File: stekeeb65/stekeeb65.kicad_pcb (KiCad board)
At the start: 2 copper layers, 303.2 x 97.6 mm, 251 parts, among them IC0 ATMEGA32U4-AU, IC1 IS31FL3733B-TQLS4, IC2 IS31FL3733B-TQLS4, J0 Conn_02x03_Odd_Even, J1 TYPE-C-31-M12_13_EDITED, SW0 SW_Push, U0 WE-TVS-82400102, Y0 16MHz

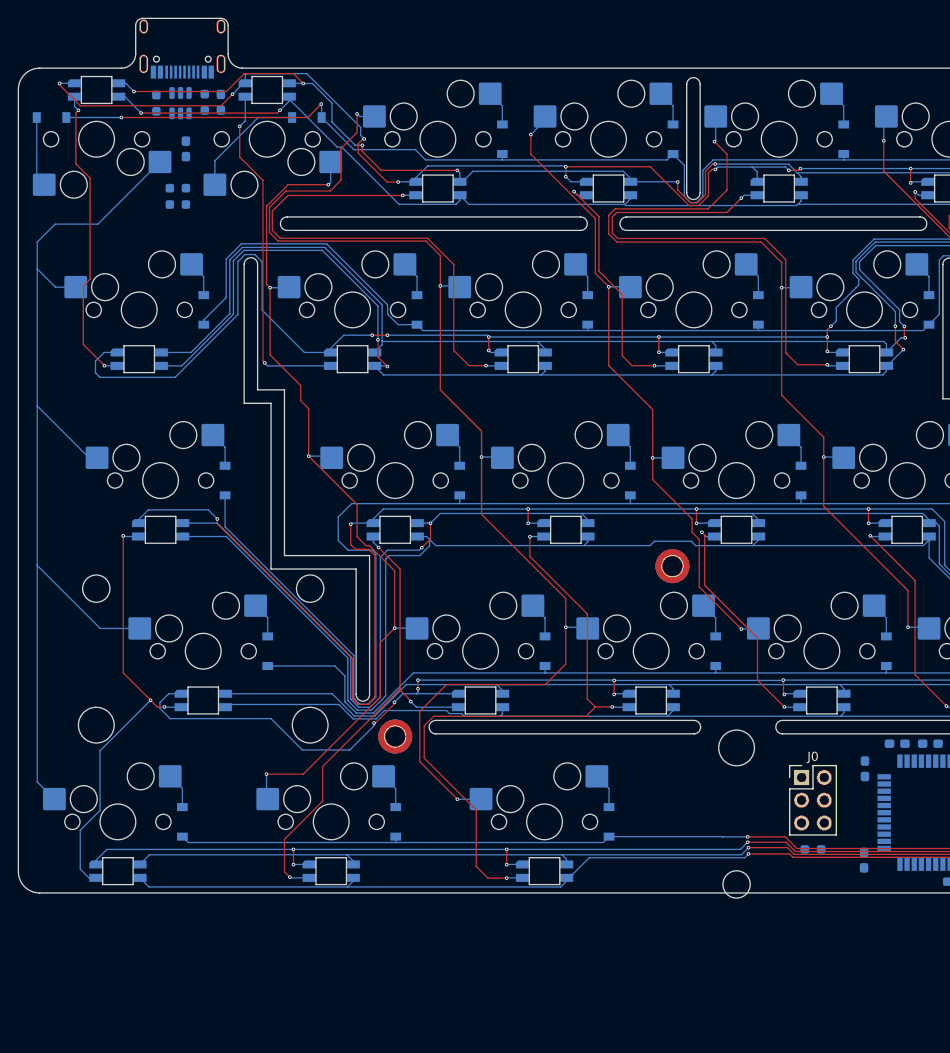
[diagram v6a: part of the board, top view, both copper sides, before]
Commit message: Replacing Type-C in lieu of a daughter board connector.
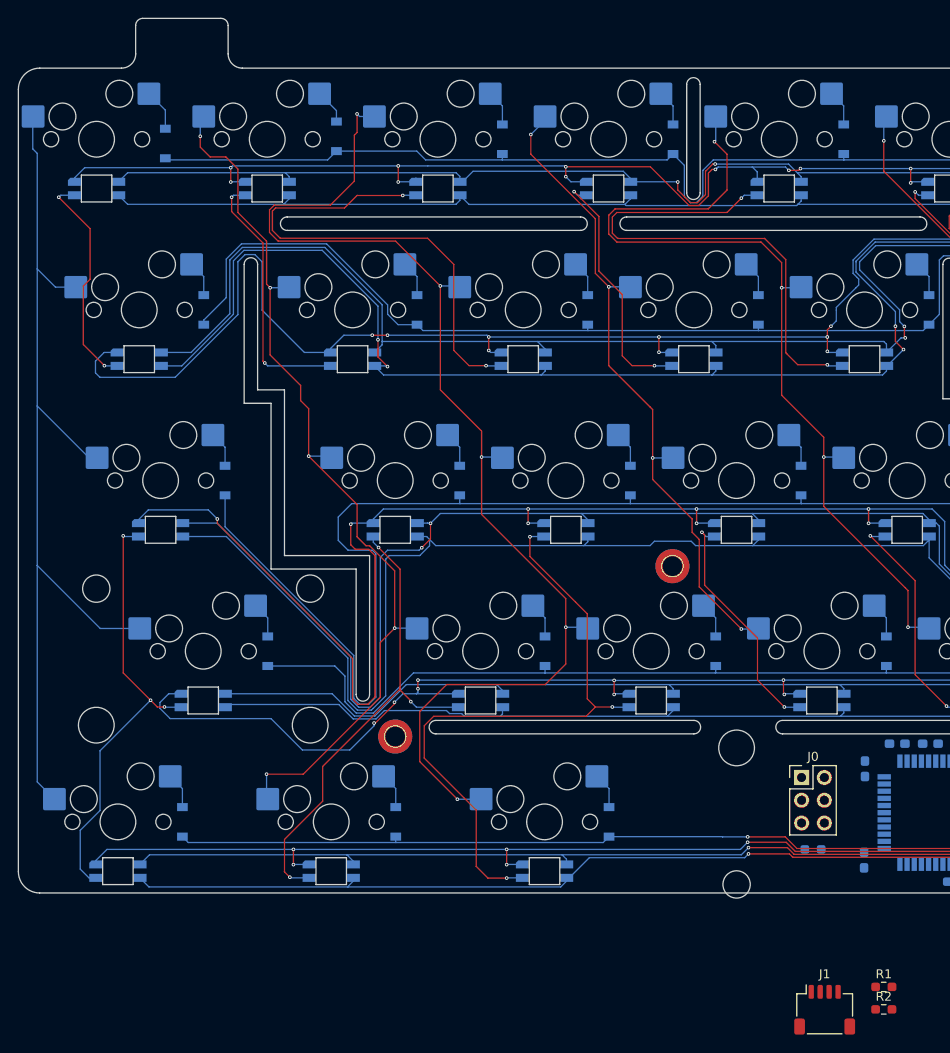
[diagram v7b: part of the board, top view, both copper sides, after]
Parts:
- removed C8: 0.1u, Capacitor_SMD:C_0603_1608Metric_Pad1.08x0.95mm_HandSolder
- removed F0: Polyfuse, Fuse:Fuse_0603_1608Metric_Pad1.05x0.95mm_HandSolder
- removed R3, R4: 5.1k, Resistor_SMD:R_0603_1608Metric_Pad0.98x0.95mm_HandSolder
- removed U0: WE-TVS-82400102, Package_TO_SOT_SMD:SOT-23-6
- J1: value TYPE-C-31-M12_13_EDITED -> Conn_01x04; footprint Type-C:HRO-TYPE-C-31-M-12-Assembly -> Connector_JST:JST_SH_SM04B-SRSS-TB_1x04-1MP_P1.00mm_Horizontal; moved to F.Cu
- R1, R2: moved to F.Cu
- moved J1 133.3 mm to (90.8, 106.7)
- moved R2 119.6 mm to (97.4, 106.7), turned to 0 degrees
- moved R1 118.9 mm to (97.4, 104.2), turned to 0 degrees
- moved D_0 13.0 mm to (17.2, 10.0), turned to 90 degrees
- moved S0 11.0 mm to (9.53, 15.0)
- moved S1 11.0 mm to (28.6, 15.0)
- moved D_1 3.91 mm to (36.3, 9.20), turned to 90 degrees
- turned K_0 to 0 degrees
- turned K_1 to 0 degrees
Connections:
- IC0 pad 3: Net-(IC0-Pad3) -> MCU_D-
- IC0 pad 4: Net-(IC0-Pad4) -> MCU_D+
- IC2 pad 34: unconnected-(IC2-Pad34) -> GND
- J1 pad 2: Net-(F0-Pad1) -> Net-(J1-Pad2)
- J1 pad 3: unconnected-(J1-Pad3) -> Net-(J1-Pad3)
- J1 pad 4: Net-(J1-Pad4) -> +5V
- R1 pad 1: MCU_D- -> Net-(J1-Pad3)
- R1 pad 2: Net-(IC0-Pad3) -> MCU_D-
- R2 pad 1: Net-(IC0-Pad4) -> MCU_D+
- R2 pad 2: MCU_D+ -> Net-(J1-Pad2)
- S55 pad 1: unconnected-(S55-Pad1) -> LED_Row_B3
- S55 pad 2: unconnected-(S55-Pad2) -> LED_Row_G3
- S55 pad 3: unconnected-(S55-Pad3) -> LED_Row_R3
- S56 pad 1: unconnected-(S56-Pad1) -> LED_Row_B3
- S56 pad 2: unconnected-(S56-Pad2) -> LED_Row_G3
- S56 pad 3: unconnected-(S56-Pad3) -> LED_Row_R3
- S62 pad 1: unconnected-(S62-Pad1) -> LED_Row_B4
- S62 pad 2: unconnected-(S62-Pad2) -> LED_Row_G4
- S62 pad 3: unconnected-(S62-Pad3) -> LED_Row_R4
- S63 pad 1: unconnected-(S63-Pad1) -> LED_Row_B4
- S63 pad 2: unconnected-(S63-Pad2) -> LED_Row_G4
- S63 pad 3: unconnected-(S63-Pad3) -> LED_Row_R4
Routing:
- net Row0: track 323.7 -> 309.5 mm, vias 2 -> 0
- net LED1_Col1: track 38.6 -> 29.1 mm
- net Net-(D_1-Pad2): track 13.3 -> 3.88 mm
- net LED1_Col0: track 33.7 -> 24.9 mm
- net LED_Row_G0: track 288.2 -> 280.5 mm, vias 6 -> 2
- net LED_Row_B0: track 315.3 -> 308.7 mm
- net LED_Row_R0: track 279.5 -> 274.5 mm, vias 2 -> 0
- net Col1: track 98.6 -> 102.3 mm
- net Net-(D_0-Pad2): track 7.85 -> 4.66 mm
- net Col0: track 109.0 -> 105.8 mm
- net Col2: track 133.5 -> 132.3 mm

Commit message: Interim commit before potentially breaking stuff
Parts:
- added D_64: D, random-keyboard-parts:D_SOD-123-Pretty, B.Cu at (245.9, 85.2)
- added K_64: KEYSW, MX_Hotswap:MX-Hotswap-1U, F.Cu at (238.1, 85.7)
- added S64: QBLP677R-RGB, random-keyboard-parts:QBLP677R-RGB-square_cutout, B.Cu at (238.1, 91.2)
- K_62, K_63: footprint MX_Hotswap:MX-Hotswap-1.25U -> MX_Hotswap:MX-Hotswap-1U
- moved K_63 7.14 mm to (219.1, 85.7)
- moved S63 7.14 mm to (219.1, 91.2)
- moved JP0 6.72 mm to (114.6, 77.9), turned to 0 degrees
- moved D_63 6.19 mm to (227.3, 84.8)
- moved J1 3.93 mm to (86.9, 106.2), turned to 90 degrees
- moved K_62 2.38 mm to (200.0, 85.7)
- moved S62 2.38 mm to (200.0, 91.2)
- moved R8 2.30 mm to (164.8, 91.9)
- moved C10 2.30 mm to (173.8, 90.3)
- moved C11 2.30 mm to (173.8, 92.0)
- moved C15 2.30 mm to (175.8, 84.3)
- moved C20 2.30 mm to (168.9, 77.8)
- moved R10 2.30 mm to (164.8, 90.3)
- moved R12 2.30 mm to (175.8, 87.8)
- moved C16 2.30 mm to (177.6, 84.3)
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- renumbered D_64 to D_65, D_65 to D_66, D_66 to D_67, K_64 to K_65, K_65 to K_66, K_66 to K_67, S64 to S65, S65 to S66, S66 to S67
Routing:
- net LED_Row_B4: track 202.7 -> 314.8 mm, vias 8 -> 19
- net Col0: track 105.8 -> 211.1 mm, vias 0 -> 6
- net Col1: track 102.3 -> 181.1 mm
- net Col7: track 73.3 -> 145.3 mm, vias 4 -> 5
- net Col2: track 132.3 -> 188.5 mm, vias 5 -> 7
- net LED2_Col11: track 1.82 -> 45.4 mm, vias 1 -> 2
- net Col4: track 99.3 -> 141.6 mm, vias 4 -> 6
- net Col3: track 74.3 -> 116.1 mm, vias 4 -> 5
- net Col11: track 47.7 -> 89.1 mm, vias 3 -> 4
- net Col6: track 130.4 -> 153.4 mm
- net +5V: track 0.00 -> 22.5 mm
- net LED2_Col10: track 64.3 -> 70.8 mm
- net Net-(D_63-Pad2): track 3.99 -> 0.00 mm
- net Row4: track 278.9 -> 282.8 mm
- net Net-(D_64-Pad2): track 0.00 -> 3.71 mm
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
